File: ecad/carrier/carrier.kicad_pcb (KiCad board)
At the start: 4 copper layers, 76 x 58 mm, 121 parts, among them J1 XT30PW-M battery, J10 Servo chain 2, J11 Servo chain 3, J12 Servo chain 3, J13 Speaker CMS-18132-18SP, J14 Head board, J2 Cell sense: MID, NTC, J3 Main switch, J4 USB-C charge, J5 Radxa ZERO 3W, J6 Debug UART, J7 Servo chain 1, J8 Servo chain 1, J9 Servo chain 2, U1 TPS259824LNRGE, U10 MAX98357AETE+T, U11 BNO085, U2 TPS56C215RNNR, U3 TPS62933DRLR, U4 TLV75533PDBVR, U5 BQ25887RGER, U6 ADS1115IDGSR, U7 74LVC2G241DCUR, U8 74LVC2G241DCUR, U9 74LVC2G241DCUR

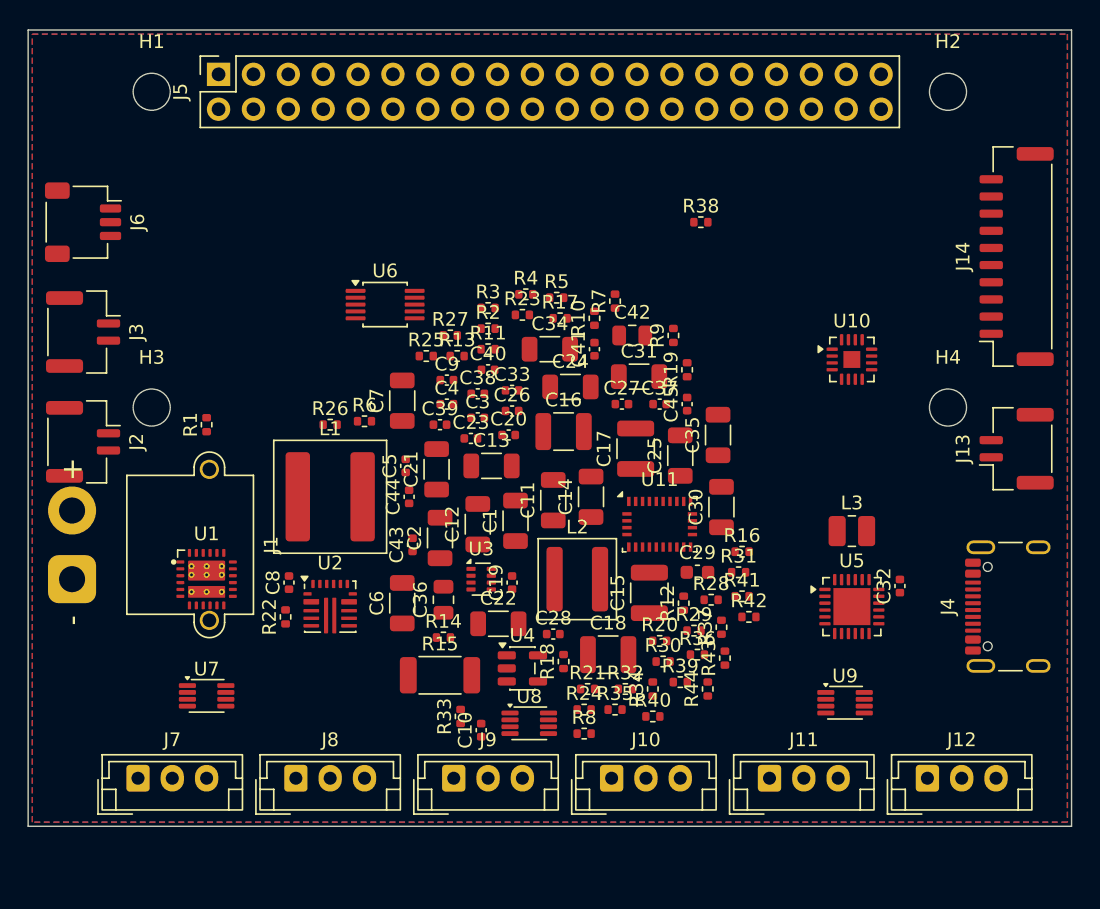
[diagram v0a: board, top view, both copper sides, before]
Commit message: Phase 2 complete: carrier board PCB, harness, DCK-02 rev A
- Generated 4-layer 76 x 62 mm carrier PCB: placement, Freerouting, power
  pours and stitching; DRC 0 violations, 0 unconnected, 0 parity issues
- STEP export for Fusion, renders, end-to-end build script
- Harness definition from params.py with service loops per joint travel
- Asset register, CLAUDE.md and README updated; head board deferred (RK9)

Co-Authored-By: Claude Opus 5.5 <noreply@anthropic.com>
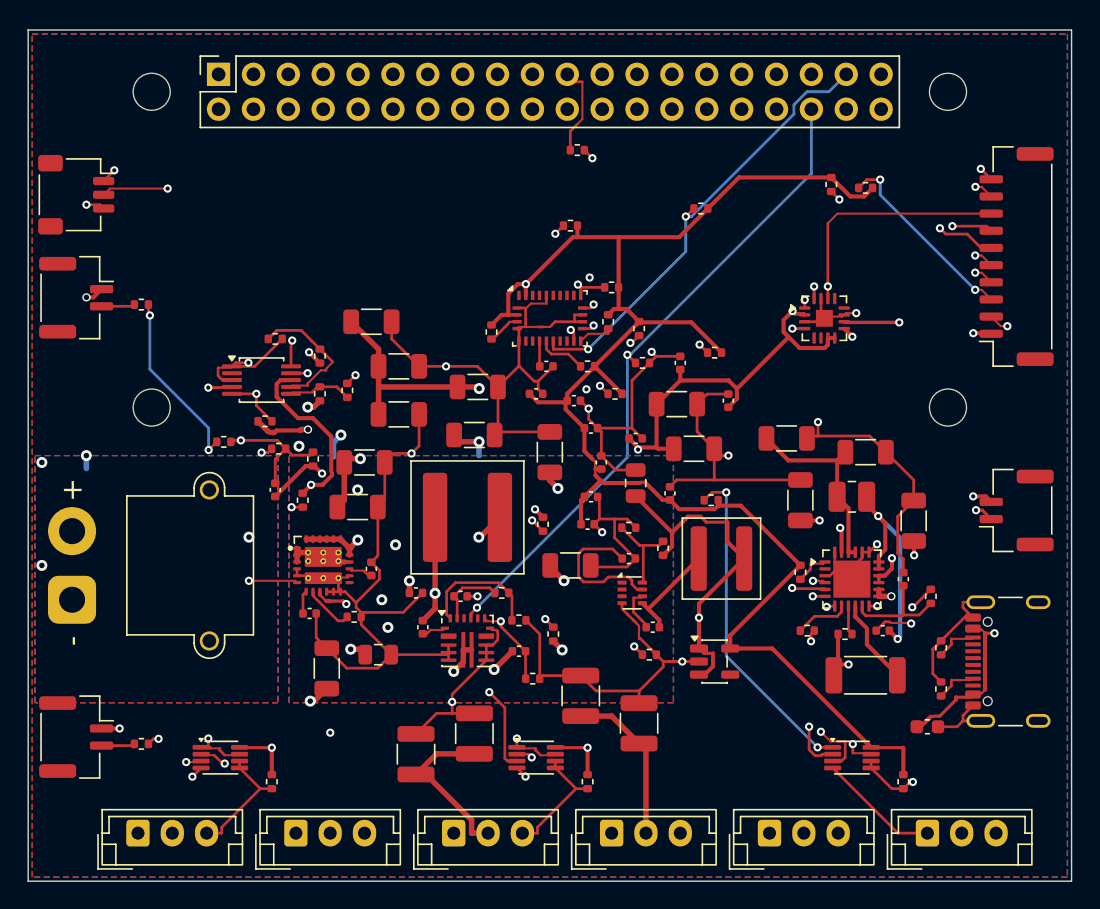
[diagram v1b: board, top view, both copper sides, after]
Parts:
- C1, C11, C12, C13, C14, C2, C21, C22, C24, C25, C30, C31, C34, C35, C6, C7: footprint C_1206_3216Metric -> Capacitor_SMD:C_1206_3216Metric
- C10, C19, C20, C23, C26, C27, C28, C3, C32, C33, C37, C38, C39, C4, C40, C41, C43, C44, C45, C5, C8, C9: footprint C_0402_1005Metric -> Capacitor_SMD:C_0402_1005Metric
- C15, C16, C17, C18: footprint C_1210_3225Metric -> Capacitor_SMD:C_1210_3225Metric
- C29: footprint C_0603_1608Metric -> Capacitor_SMD:C_0603_1608Metric
- C36, C42: footprint C_0805_2012Metric -> Capacitor_SMD:C_0805_2012Metric
- H1, H2, H3, H4: footprint MountingHole_2.7mm_M2.5 -> MountingHole:MountingHole_2.7mm_M2.5
- J1: footprint AMASS_XT30PW-M_1x02_P2.50mm_Horizontal -> Connector_AMASS:AMASS_XT30PW-M_1x02_P2.50mm_Horizontal
- J10, J11, J12, J7, J8, J9: footprint JST_EH_B3B-EH-A_1x03_P2.50mm_Vertical -> Connector_JST:JST_EH_B3B-EH-A_1x03_P2.50mm_Vertical
- J13, J2, J3: footprint JST_GH_SM02B-GHS-TB_1x02-1MP_P1.25mm_Horizontal -> Connector_JST:JST_GH_SM02B-GHS-TB_1x02-1MP_P1.25mm_Horizontal
- J14: footprint JST_GH_SM10B-GHS-TB_1x10-1MP_P1.25mm_Horizontal -> Connector_JST:JST_GH_SM10B-GHS-TB_1x10-1MP_P1.25mm_Horizontal
- J4: footprint USB_C_Receptacle_GCT_USB4105-xx-A_16P_TopMnt_Horizontal -> Connector_USB:USB_C_Receptacle_GCT_USB4105-xx-A_16P_TopMnt_Horizontal
- J5: footprint PinSocket_2x20_P2.54mm_Vertical -> Connector_PinSocket_2.54mm:PinSocket_2x20_P2.54mm_Vertical
- J6: footprint JST_SH_SM03B-SRSS-TB_1x03-1MP_P1.00mm_Horizontal -> Connector_JST:JST_SH_SM03B-SRSS-TB_1x03-1MP_P1.00mm_Horizontal
- L1: footprint L_Coilcraft_XAL7030-222 -> Inductor_SMD:L_Coilcraft_XAL7030-222
- L2: footprint L_Coilcraft_XAL5030-XXX -> Inductor_SMD:L_Coilcraft_XAL5030-XXX
- L3: footprint L_1008_2520Metric -> Inductor_SMD:L_1008_2520Metric
- R1, R10, R11, R12, R13, R14, R16, R17, R18, R19, R2, R20, R21, R22, R23, R24, R25, R26, R27, R28, R29, R3, R30, R31, R32, R33, R34, R35, R36, R37, R38, R39, R4, R40, R41, R42, R43, R44, R5, R6, R7, R8, R9: footprint R_0402_1005Metric -> Resistor_SMD:R_0402_1005Metric
- R15: footprint R_2010_5025Metric -> Resistor_SMD:R_2010_5025Metric
- U1: footprint Texas_RGE0024M_TPS25982 -> duccky:Texas_RGE0024M_TPS25982
- U10: footprint TQFN-16-1EP_3x3mm_P0.5mm_EP1.23x1.23mm -> Package_DFN_QFN:TQFN-16-1EP_3x3mm_P0.5mm_EP1.23x1.23mm
- U11: footprint LGA-28_5.2x3.8mm_P0.5mm -> Package_LGA:LGA-28_5.2x3.8mm_P0.5mm
- U2: footprint Texas_RNN0018A -> Package_DFN_QFN:Texas_RNN0018A
- U3: footprint SOT-583-8 -> Package_TO_SOT_SMD:SOT-583-8
- U4: footprint SOT-23-5 -> Package_TO_SOT_SMD:SOT-23-5
- U5: footprint Texas_RGE0024H_VQFN-24-1EP_4x4mm_P0.5mm_EP2.7x2.7mm -> Package_DFN_QFN:Texas_RGE0024H_VQFN-24-1EP_4x4mm_P0.5mm_EP2.7x2.7mm
- U6: footprint TSSOP-10_3x3mm_P0.5mm -> Package_SO:TSSOP-10_3x3mm_P0.5mm
- U7, U8, U9: footprint VSSOP-8_2.3x2mm_P0.5mm -> Package_SO:VSSOP-8_2.3x2mm_P0.5mm
- moved R13 41.2 mm to (66.5, 45.0), turned to 90 degrees
- moved R29 34.0 mm to (58.5, 11.2), turned to 90 degrees
- moved R28 32.0 mm to (61.0, 11.5)
- moved C33 31.6 mm to (63.8, 40.0), turned to 90 degrees
- moved R18 31.3 mm to (8.25, 52.0), turned to 0 degrees
- moved R42 31.3 mm to (39.5, 14.2)
- moved R15 31.0 mm to (61.0, 47.0)
- moved R24 30.0 mm to (21.2, 26.5), turned to 90 degrees
- moved C34 29.3 mm to (64.5, 35.8), turned to 90 degrees
- moved R14 29.3 mm to (59.5, 44.0)
- moved R39 29.0 mm to (33.8, 22.0), turned to 90 degrees
- moved R41 28.4 mm to (49.0, 13.0)
- moved R30 27.5 mm to (42.5, 18.8)
- moved R32 27.2 mm to (20.0, 34.2), turned to 90 degrees
- moved R9 27.0 mm to (36.8, 47.2), turned to 0 degrees
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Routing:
- net /GND: track 0.00 -> 254.5 mm, vias 0 -> 21
- net /3V3: track 0.00 -> 218.9 mm, vias 0 -> 5
- net /V5_SYS: track 0.00 -> 132.4 mm, vias 0 -> 4
- net /BAT_MID: track 0.00 -> 92.4 mm, vias 0 -> 4
- net /I2C4_SDA: track 0.00 -> 90.2 mm, vias 0 -> 3
- net /VBAT: track 0.00 -> 88.9 mm, vias 0 -> 8
- net /I2C4_SCL: track 0.00 -> 72.5 mm, vias 0 -> 4
- net /CHG_TS: track 0.00 -> 70.9 mm, vias 0 -> 4
- net /BUS3_DIR: track 0.00 -> 69.9 mm, vias 0 -> 4
- net /BUS1_DIR: track 0.00 -> 61.7 mm, vias 0 -> 2
- net /BUS2_DIR: track 0.00 -> 60.9 mm, vias 0 -> 2
- net /UART5_RX: track 0.00 -> 54.3 mm, vias 0 -> 1
- net /UART3_TX: track 0.00 -> 54.1 mm, vias 0 -> 1
- net /UART3_RX: track 0.00 -> 53.2 mm, vias 0 -> 1
- net /I2S_SCLK: track 0.00 -> 52.5 mm, vias 0 -> 2
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- added copper zone on B.Cu, net /GND
- added copper zone on F.Cu, net /GND
- added copper zone on In1.Cu, net /GND
- added copper zone on In2.Cu, net /V5_SERVO
- added copper zone on B.Cu, net /VBAT
- added copper zone on F.Cu, net /VBAT
- added copper zone on B.Cu, net /VSYS
- added copper zone on F.Cu, net /VSYS
- removed copper zone on B.Cu, net (none)
- removed copper zone on F.Cu, net (none)
- removed copper zone on In1.Cu, net (none)
- removed copper zone on In2.Cu, net (none)
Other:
- board size 76 x 58 mm -> 76 x 62 mm

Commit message: Carrier: exact Radxa hole and header positions, 3D body substitutions, iterative dangling cleanup; leg layout study
Co-Authored-By: Claude Opus 5.5 <noreply@anthropic.com>
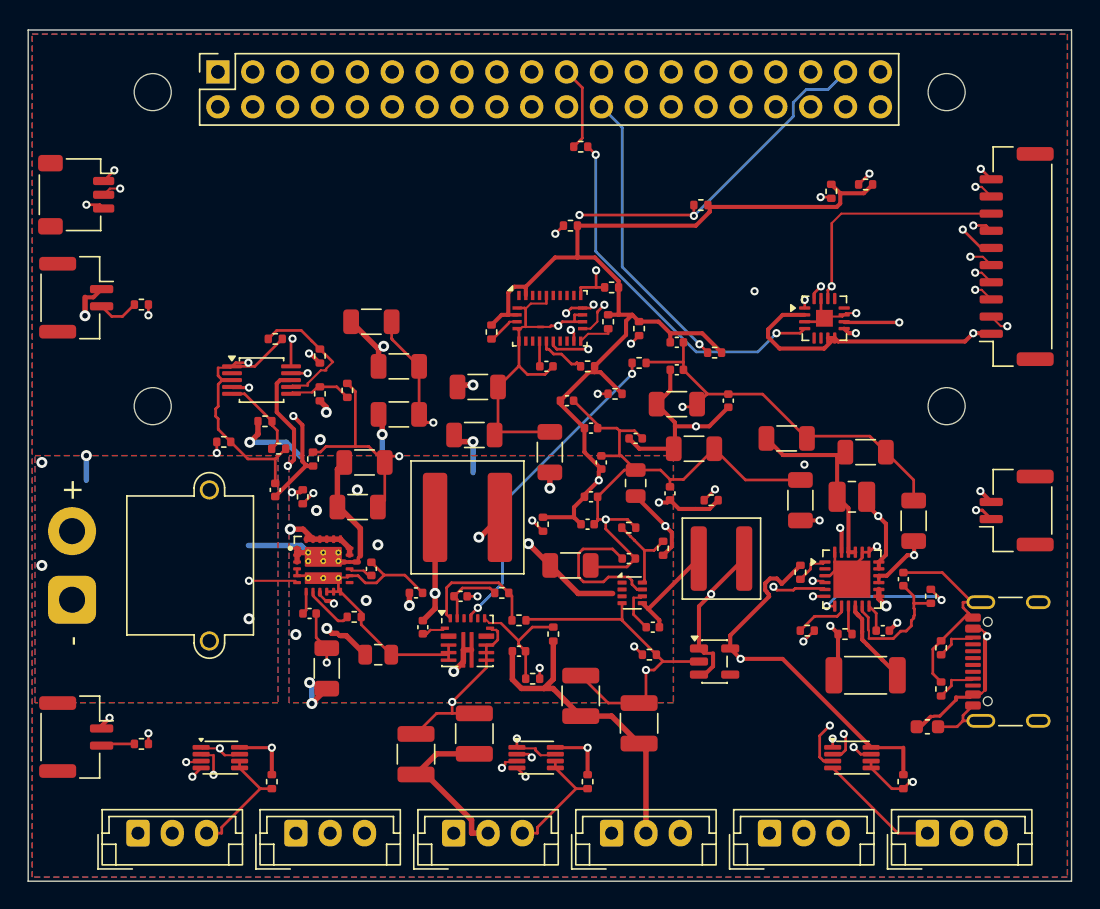
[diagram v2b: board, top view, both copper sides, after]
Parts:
- moved C44 10.9 mm to (47.2, 22.8)
- moved C26 0.56 mm to (47.2, 24.8), turned to 0 degrees
- moved C40 0.50 mm to (39.2, 27.0)
- moved R29 0.50 mm to (58.5, 11.8)
- moved R38 0.35 mm to (40.2, 8.50)
- moved R28 0.25 mm to (61.0, 11.2)
- moved R32 0.25 mm to (20.0, 34.0)
- moved R41 0.25 mm to (49.0, 12.8)
- moved R5 0.25 mm to (44.5, 24.2)
- moved J5 0.18 mm to (13.8, 3.06)
- moved H4 0.14 mm to (66.9, 27.4)
- moved H3 0.13 mm to (9.07, 27.4)
- moved H2 0.10 mm to (66.9, 4.53)
- moved H1 0.08 mm to (9.07, 4.53)
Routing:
- net /3V3: track 218.9 -> 204.8 mm, vias 5 -> 7
- net /AMP_SDMODE: track 37.8 -> 26.8 mm
- net /V5_SERVO: track 33.4 -> 42.8 mm, vias 5 -> 3
- net /BAT_MID: track 92.4 -> 84.1 mm, vias 4 -> 3
- net /I2C4_SCL: track 72.5 -> 80.5 mm, vias 4 -> 5
- net /VSYS: track 40.5 -> 47.7 mm, vias 13 -> 16
- net /CHG_INT: track 49.8 -> 43.8 mm, vias 3 -> 2
- net /V5_SYS: track 132.4 -> 138.4 mm
- net /I2S_LRCK: track 41.9 -> 36.4 mm
- net /UART3_RX: track 53.2 -> 58.6 mm
- net /IMU_RST: track 32.9 -> 38.1 mm, vias 2 -> 3
- net /I2C4_SDA: track 90.2 -> 94.8 mm, vias 3 -> 4
- net /CHG_BTST: track 6.48 -> 2.00 mm, vias 2 -> 0
- net /I2S_SCLK: track 52.5 -> 56.8 mm
- net /VSYS_SENSE: track 9.54 -> 6.07 mm, vias 2 -> 0
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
